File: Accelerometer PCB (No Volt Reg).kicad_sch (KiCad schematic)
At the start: 21 parts, among them J1 S2B-PH-SM4-TB_LF__SN_, J2 M20-8770442, J3 MolexMicroSD, SW1 SW_Push, SW2 SW_Push, U1 Swan v3.0, U2 Sysrox Accelerometer, U3 Adafruit DS3231 RTC

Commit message: Add files via upload
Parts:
- removed C7: 10uF, Local Accelerometer Footprints:10uF External Input Cap, symbol Device:C
- added C1: 100uF, Local Accelerometer Footprints:BulkCap, symbol Device:C
- C2: value 100uF -> 100nf; footprint Local Accelerometer Footprints:BulkCap -> Local Accelerometer Footprints:Large Decoupling Capacitor
- C3: value 100nf -> 100nF
- C6: value 100nF -> 10uF; footprint Local Accelerometer Footprints:Large Decoupling Capacitor -> Local Accelerometer Footprints:10uF External Input Cap
- J1: value S2B-PH-SM4-TB_LF__SN_ -> Power Connector
- R1, R2: value 100k -> 100kΩ
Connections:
- net GND: now also C2.1, C3.2, C6.1, J3.4 (VDD), C1.2; no longer C2.2, C3.1, C6.2, J3.6 (VSS)
- net at J3.1 (DAT2): now also R1.2; no longer R1.1
- net +3.3V: now reaches C4.1, C5.1, J2.3 (VCC), R2.2, U1.2 (3V3_REG_OUT), U2.1 (3V3), U3.1 (VCC)
- net +3.3V: now also C2.2, C3.1, C6.2, J3.6 (VSS), R1.1; no longer C3.2, C6.1, J3.4 (VDD), R1.2
- net Input Power: now reaches D1.1 (K), U1.3 (VIN)
- net Input Power: now also C1.1; no longer C2.1
- net OLED Serial Data: now reaches J2.1 (SDA), U1.40 (SDA2)
- net OLED Serial Clock: now reaches J2.2 (SCL), U1.42 (SCL2)
- net Switch 2 I/O: now reaches SW2.2, U1.10 (A2)
- net 32kHz Frame Sync: now reaches U2.3 (FSY), U3.6 (32K)
- net IMU Interrupt: now reaches U1.47 (D6), U2.4 (INT)
- net IMU MISO: now reaches U1.55 (D12), U2.5 (MISO)
- net IMU MOSI: now reaches U1.53 (D11), U2.6 (MOSI)
- net IMU Serial Clock: now reaches U1.57 (D13), U2.7 (CLK)
- net IMU Chip Select: now reaches U1.51 (D10), U2.8 (CS)
- net MicroSD Clock Line: now reaches J3.5 (CLK), U1.18 (SCK)
- net MicroSD MOSI: now reaches J3.3 (CMD), U1.20 (MOSI)
- net MicroSD MISO: now reaches J3.7 (DA0), U1.22 (MISO)
- net RTC Data Line: now reaches U1.41 (SDA), U3.4 (SDA)
- net RTC Clock Line: now reaches U1.43 (SCL), U3.3 (SCL)
- net RTC Square Wave: now reaches U1.46 (D8), U3.7 (SQW)
- net MicroSD Card Detect: now reaches J3.2 (CD/DAT3), U1.49 (D9)
- net Switch 1 I/O: now reaches SW1.2, U1.8 (A1)
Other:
- note added: "6DOF icm42688 Inertial Motion Unit"
- note added: "Adafruit DS3231 Real-Time Clock Breakout Board"
- note added: "Blues Swan v3.0 Microcontroller"
- note added: "Input Stage"
- note added: "M20-8770442 OLED Screen 4 pin Connector"
- note added: "MicroSD Card Slot"
- note added: "Mounting Holes"
- note added: "Push Button Switches"

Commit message: Updated Project Files
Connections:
- net +3.3V: now also J3.4 (VDD); no longer J3.6 (VSS)
- net GND: now also J3.6 (VSS); no longer J3.4 (VDD)
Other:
- moved on the sheet: C3, C6
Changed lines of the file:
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@@
 	)
 	(junction
-		(at 67.31 106.68)
+		(at 77.47 99.06)
 		(diameter 0)
 		(color 0 0 0 0)
 	)
 	(junction
-		(at 245.11 96.52)
+		(at 67.31 106.68)
 		(diameter 0)
 		(color 0 0 0 0)
 	)
 	(junction
-		(at 77.47 99.06)
+		(at 245.11 96.52)
 		(diameter 0)
 		(color 0 0 0 0)
@@
 	)
 	(junction
+		(at 88.9 106.68)
+		(diameter 0)
+		(color 0 0 0 0)
+	)
+	(junction
 		(at 54.61 68.58)
 		(diameter 0)
@@
 	)
 	(junction
-		(at 245.11 88.9)
+		(at 67.31 99.06)
 		(diameter 0)
 		(color 0 0 0 0)
 	)
 	(junction
-		(at 77.47 106.68)
+		(at 245.11 88.9)
 		(diameter 0)
 		(color 0 0 0 0)
 	)
 	(junction
-		(at 40.64 102.87)
+		(at 77.47 106.68)
 		(diameter 0)
 		(color 0 0 0 0)
 	)
 	(junction
-		(at 209.55 62.23)
+		(at 40.64 102.87)
 		(diameter 0)
 		(color 0 0 0 0)
 	)
 	(junction
-		(at 88.9 99.06)
+		(at 209.55 62.23)
 		(diameter 0)
 		(color 0 0 0 0)
@@
 		(color 0 0 0 0)
 	)
-	(junction
-		(at 67.31 99.06)
-		(diameter 0)
-		(color 0 0 0 0)
-	)
 	(no_connect
 		(at 165.1 118.11)
@@
 	(wire
 		(pts
-			(xy 88.9 99.06) (xy 90.17 99.06)
+			(xy 88.9 106.68) (xy 90.17 106.68)
 		)
 		(stroke
@@
 	(wire
 		(pts
+			(xy 77.47 106.68) (xy 88.9 106.68)
+		)
+		(stroke
+			(width 0)
+			(type default)
+		)
+	)
+	(wire
+		(pts
 			(xy 217.17 69.85) (xy 209.55 69.85)
 		)
@@
 	(wire
 		(pts
-			(xy 77.47 99.06) (xy 88.9 99.06)
-		)
-		(stroke
-			(width 0)
-			(type default)
-		)
-	)
-	(wire
-		(pts
 			(xy 60.96 104.14) (xy 64.77 104.14)
 		)
@@
 	(wire
 		(pts
-			(xy 88.9 93.98) (xy 88.9 111.76)
+			(xy 88.9 93.98) (xy 88.9 106.68)
 		)
 		(stroke
@@
 	(wire
 		(pts
-			(xy 67.31 99.06) (xy 77.47 99.06)
-		)
-		(stroke
-			(width 0)
-			(type default)
-		)
-	)
-	(wire
-		(pts
 			(xy 82.55 134.62) (xy 86.36 134.62)
 		)
@@
 	(wire
 		(pts
-			(xy 67.31 106.68) (xy 77.47 106.68)
+			(xy 40.64 139.7) (xy 40.64 143.51)
 		)
 		(stroke
@@
 	(wire
 		(pts
-			(xy 40.64 139.7) (xy 40.64 143.51)
+			(xy 215.9 58.42) (xy 215.9 53.34)
 		)
 		(stroke
@@
 	(wire
 		(pts
-			(xy 215.9 58.42) (xy 215.9 53.34)
+			(xy 245.11 96.52) (xy 255.27 96.52)
 		)
 		(stroke
@@
 	(wire
 		(pts
-			(xy 245.11 96.52) (xy 255.27 96.52)
+			(xy 219.71 66.04) (xy 217.17 66.04)
 		)
 		(stroke
@@
 	(wire
 		(pts
-			(xy 219.71 66.04) (xy 217.17 66.04)
+			(xy 165.1 105.41) (xy 168.91 105.41)
 		)
 		(stroke
@@
 	(wire
 		(pts
-			(xy 165.1 105.41) (xy 168.91 105.41)
+			(xy 88.9 106.68) (xy 88.9 111.76)
 		)
 		(stroke
@@
 	(wire
 		(pts
+			(xy 67.31 99.06) (xy 77.47 99.06)
+		)
+		(stroke
+			(width 0)
+			(type default)
+		)
+	)
+	(wire
+		(pts
 			(xy 72.39 144.78) (xy 68.58 144.78)
 		)
@@
 	(wire
 		(pts
+			(xy 67.31 106.68) (xy 77.47 106.68)
+		)
+		(stroke
+			(width 0)
+			(type default)
+		)
+	)
+	(wire
+		(pts
 			(xy 67.31 60.96) (xy 71.12 60.96)
 		)
@@
 	(wire
 		(pts
-			(xy 77.47 106.68) (xy 82.55 106.68)
+			(xy 40.64 139.7) (xy 52.07 139.7)
 		)
 		(stroke
@@
 	(wire
 		(pts
-			(xy 40.64 139.7) (xy 52.07 139.7)
+			(xy 73.66 93.98) (xy 88.9 93.98)
 		)
 		(stroke
@@
 	(wire
 		(pts
-			(xy 73.66 93.98) (xy 88.9 93.98)
+			(xy 77.47 99.06) (xy 82.55 99.06)
 		)
 		(stroke
@@
 	(symbol
 		(lib_id "Device:C")
-		(at 67.31 102.87 180)
+		(at 67.31 102.87 0)
 		(unit 1)
 		(body_style 1)
@@
 		(dnp no)
 		(property "Reference" "C6"
-			(at 69.85 101.6 0)
+			(at 70.104 101.6 0)
 			(show_name no)
 			(do_not_autoplace no)
@@
 					(size 1.27 1.27)
 				)
-				(justify right)
+				(justify left)
 			)
 		)
 		(property "Value" "10uF"
-			(at 69.85 104.14 0)
+			(at 70.104 104.14 0)
 			(show_name no)
 			(do_not_autoplace no)
@@
 					(size 1.27 1.27)
 				)
-				(justify right)
+				(justify left)
 			)
 		)
 		(property "Footprint" "Local Accelerometer Footprints:10uF External Input Cap"
-			(at 66.3448 99.06 0)
+			(at 68.2752 106.68 0)
 			(hide yes)
 			(show_name no)
@@
 	(symbol
 		(lib_id "power:+3.3V")
-		(at 90.17 99.06 270)
+		(at 90.17 106.68 270)
 		(unit 1)
 		(body_style 1)
@@
 		(dnp no)
 		(property "Reference" "#PWR06"
-			(at 86.36 99.06 0)
+			(at 86.36 106.68 0)
 			(hide yes)
 			(show_name no)
@@
 		)
 		(property "Value" "+3.3V"
-			(at 92.964 99.06 90)
+			(at 92.964 106.68 90)
 			(show_name no)
 			(do_not_autoplace no)
@@
 		)
 		(property "Footprint" ""
-			(at 90.17 99.06 0)
+			(at 90.17 106.68 0)
 			(hide yes)
 			(show_name no)
@@
 		)
 		(property "Datasheet" ""
-			(at 90.17 99.06 0)
+			(at 90.17 106.68 0)
 			(hide yes)
 			(show_name no)
@@
 		)
 		(property "Description" "Power symbol creates a global label with name \"+3.3V\""
-			(at 90.17 99.06 0)
+			(at 90.17 106.68 0)
 			(hide yes)
 			(show_name no)
@@
 	(symbol
 		(lib_id "Device:C")
-		(at 77.47 102.87 0)
+		(at 77.47 102.87 180)
 		(unit 1)
 		(body_style 1)
@@
 					(size 1.27 1.27)
 				)
-				(justify left)
+				(justify right)
 			)
 		)
@@
 					(size 1.27 1.27)
 				)
-				(justify left)
+				(justify right)
 			)
 		)
 		(property "Footprint" "Local Accelerometer Footprints:Large Decoupling Capacitor"
-			(at 78.4352 106.68 0)
+			(at 76.5048 99.06 0)
 			(hide yes)
 			(show_name no)
@@
 	(symbol
 		(lib_id "power:GND")
-		(at 82.55 106.68 0)
+		(at 82.55 99.06 180)
 		(unit 1)
 		(body_style 1)
@@
 		(dnp no)
 		(property "Reference" "#PWR07"
-			(at 82.55 113.03 0)
+			(at 82.55 92.71 0)
 			(hide yes)
 			(show_name no)
@@
 		)
 		(property "Value" "GND"
-			(at 82.55 110.744 0)
+			(at 82.55 94.996 0)
 			(show_name no)
 			(do_not_autoplace no)
@@
 		)
 		(property "Footprint" ""
-			(at 82.55 106.68 0)
+			(at 82.55 99.06 0)
 			(hide yes)
 			(show_name no)
@@
 		)
 		(property "Datasheet" ""
-			(at 82.55 106.68 0)
+			(at 82.55 99.06 0)
 			(hide yes)
 			(show_name no)
@@
 		)
 		(property "Description" "Power symbol creates a global label with name \"GND\" , ground"
-			(at 82.55 106.68 0)
+			(at 82.55 99.06 0)
 			(hide yes)
 			(show_name no)

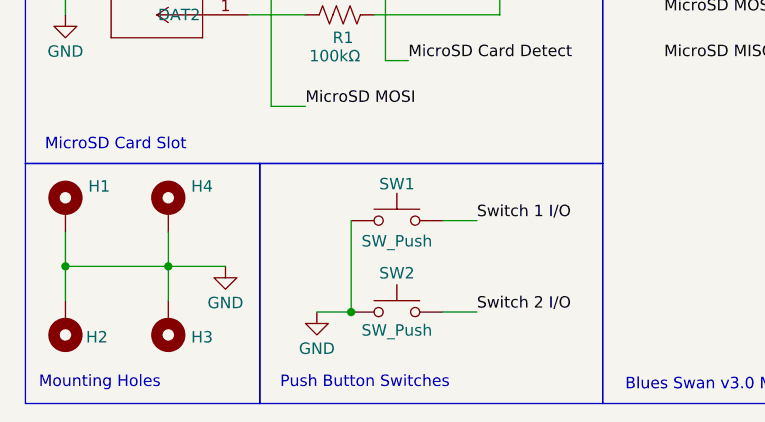
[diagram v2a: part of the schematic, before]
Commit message: Updated Screw Hole Connections and Labels
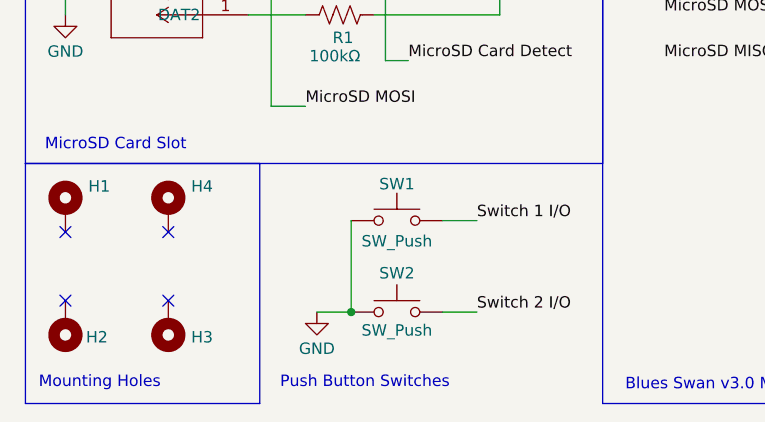
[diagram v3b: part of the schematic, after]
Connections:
- net GND: no longer H1.1, H2.1, H3.1, H4.1
- no-connect marks 48 -> 52
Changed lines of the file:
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@@
 	)
 	(rectangle
-		(start 62.23 128.27)
-		(end 100.33 154.94)
-		(stroke
-			(width 0)
-			(type default)
-		)
-		(fill
-			(type none)
-		)
-	)
-	(rectangle
 		(start 191.77 116.205)
 		(end 240.665 142.875)
@@
 	)
 	(junction
-		(at 52.07 139.7)
-		(diameter 0)
-		(color 0 0 0 0)
-	)
-	(junction
 		(at 224.79 125.73)
 		(diameter 0)
@@
 	)
 	(junction
-		(at 40.64 139.7)
-		(diameter 0)
-		(color 0 0 0 0)
-	)
-	(junction
 		(at 71.12 68.58)
 		(diameter 0)
@@
 	)
 	(no_connect
+		(at 40.64 143.51)
+	)
+	(no_connect
+		(at 52.07 135.89)
+	)
+	(no_connect
 		(at 165.1 82.55)
 	)
@@
 	)
 	(no_connect
+		(at 52.07 143.51)
+	)
+	(no_connect
 		(at 121.92 132.08)
 	)
@@
 	)
 	(no_connect
+		(at 40.64 135.89)
+	)
+	(no_connect
 		(at 143.51 52.07)
 	)
@@
 	(wire
 		(pts
-			(xy 52.07 139.7) (xy 52.07 143.51)
-		)
-		(stroke
-			(width 0)
-			(type default)
-		)
-	)
-	(wire
-		(pts
 			(xy 210.82 83.82) (xy 215.9 83.82)
 		)
@@
 	(wire
 		(pts
-			(xy 52.07 139.7) (xy 58.42 139.7)
-		)
-		(stroke
-			(width 0)
-			(type default)
-		)
-	)
-	(wire
-		(pts
-			(xy 40.64 139.7) (xy 40.64 143.51)
-		)
-		(stroke
-			(width 0)
-			(type default)
-		)
-	)
-	(wire
-		(pts
 			(xy 215.9 58.42) (xy 215.9 53.34)
 		)
@@
 	(wire
 		(pts
-			(xy 40.64 135.89) (xy 40.64 139.7)
-		)
-		(stroke
-			(width 0)
-			(type default)
-		)
-	)
-	(wire
-		(pts
-			(xy 40.64 139.7) (xy 52.07 139.7)
-		)
-		(stroke
-			(width 0)
-			(type default)
-		)
-	)
-	(wire
-		(pts
 			(xy 73.66 93.98) (xy 88.9 93.98)
 		)
@@
 	(wire
 		(pts
-			(xy 52.07 135.89) (xy 52.07 139.7)
-		)
-		(stroke
-			(width 0)
-			(type default)
-		)
-	)
-	(wire
-		(pts
 			(xy 165.1 110.49) (xy 171.45 110.49)
 		)
@@
 					(unit 1)
 				)
-			)
-		)
-	)
-	(symbol
-		(lib_id "power:GND")
-		(at 58.42 139.7 0)
-		(unit 1)
-		(body_style 1)
-		(exclude_from_sim no)
-		(in_bom yes)
-		(on_board yes)
-		(in_pos_files yes)
-		(dnp no)
-		(property "Reference" "#PWR014"
-			(at 58.42 146.05 0)
-			(hide yes)
-			(show_name no)
-			(do_not_autoplace no)
-			(effects
-				(font
-					(size 1.27 1.27)
-				)
-			)
-		)
-		(property "Value" "GND"
-			(at 58.42 143.764 0)
-			(show_name no)
-			(do_not_autoplace no)
-			(effects
-				(font
-					(size 1.27 1.27)
-				)
-			)
-		)
-		(property "Footprint" ""
-			(at 58.42 139.7 0)
-			(hide yes)
-			(show_name no)
-			(do_not_autoplace no)
-			(effects
-				(font
-					(size 1.27 1.27)
-				)
-			)
-		)
-		(property "Datasheet" ""
-			(at 58.42 139.7 0)
-			(hide yes)
-			(show_name no)
-			(do_not_autoplace no)
-			(effects
-				(font
-					(size 1.27 1.27)
-				)
-			)
-		)
-		(property "Description" "Power symbol creates a global label with name \"GND\" , ground"
-			(at 58.42 139.7 0)
-			(hide yes)
-			(show_name no)
-			(do_not_autoplace no)
-			(effects
-				(font
-					(size 1.27 1.27)
-				)
-			)
-		)
-		(pin "1"
-		)
-		(instances
-			(project "Accelerometer PCB (No Volt Reg)"
-				(path "/3063477e-972a-487a-8c68-dcb59f1864f0"
-					(reference "#PWR014")
-					(unit 1)
-				)
